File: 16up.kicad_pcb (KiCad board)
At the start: 2 copper layers, 60.8 x 99.9 mm, 38 parts, among them CN1 EXPANSION_PORT, CN2 ALMOST_USERPORT, CN3 DB9_MALE, J1 ATTENTION_IN, J2 TAPE_IN, U1 GAL20V8, U102 74LS652, U2 MOS_6529, U3 MOS_6551_ACIA, U4 MAX238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

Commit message: ExtraUserPort -> 16up
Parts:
- CN1: footprint ExtraUserPort:C16_Cart_Conn -> 16up:C16_Cart_Conn
- CN2: footprint ExtraUserPort:24Pin_Edge -> 16up:24Pin_Edge
- CN3: footprint ExtraUserPort:DB_9M -> 16up:DB_9M
- J2: footprint ExtraUserPort:Connector_Mini-DIN_Female_8Pin_2rows -> 16up:Connector_Mini-DIN_Female_8Pin_2rows
- V0: footprint ExtraUserPort:logo -> 16up:logo
- V1: footprint ExtraUserPort:cc_by_nc_sa -> 16up:cc_by_nc_sa

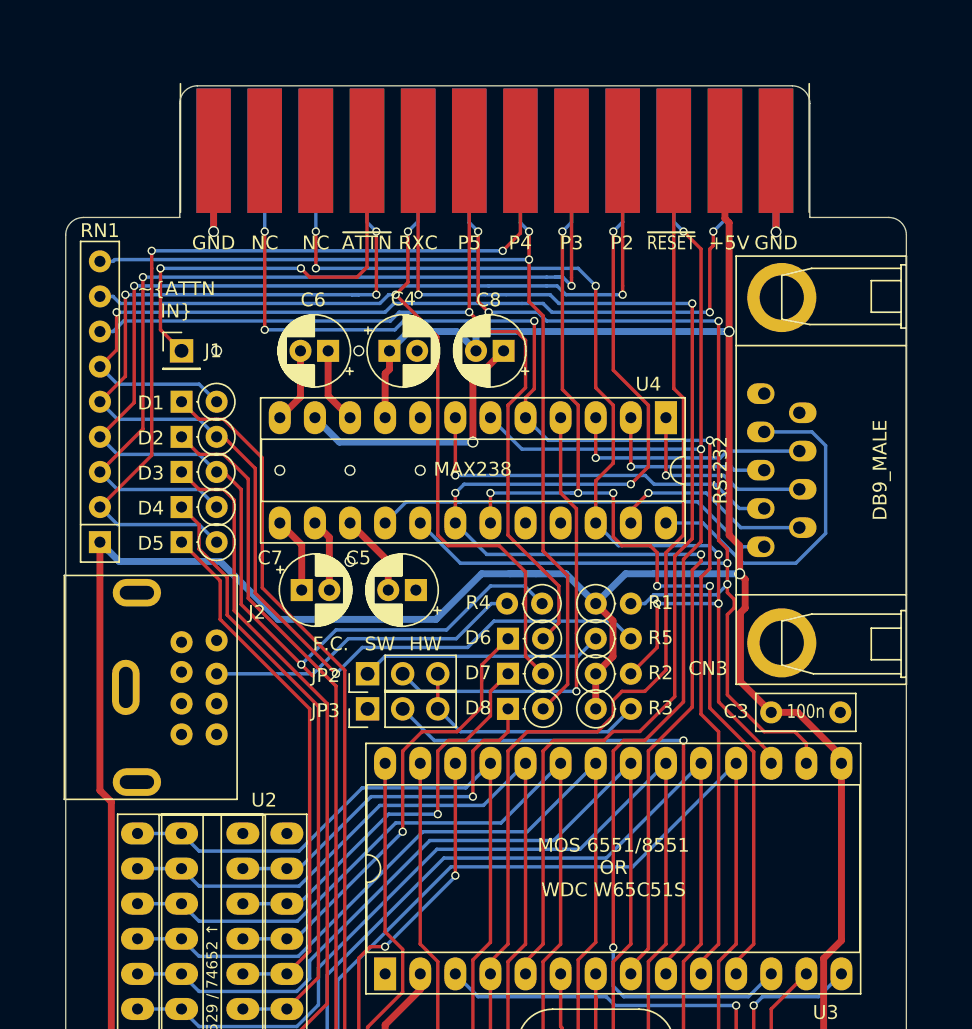
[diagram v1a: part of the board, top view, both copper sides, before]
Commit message: Fix userport connector !!!
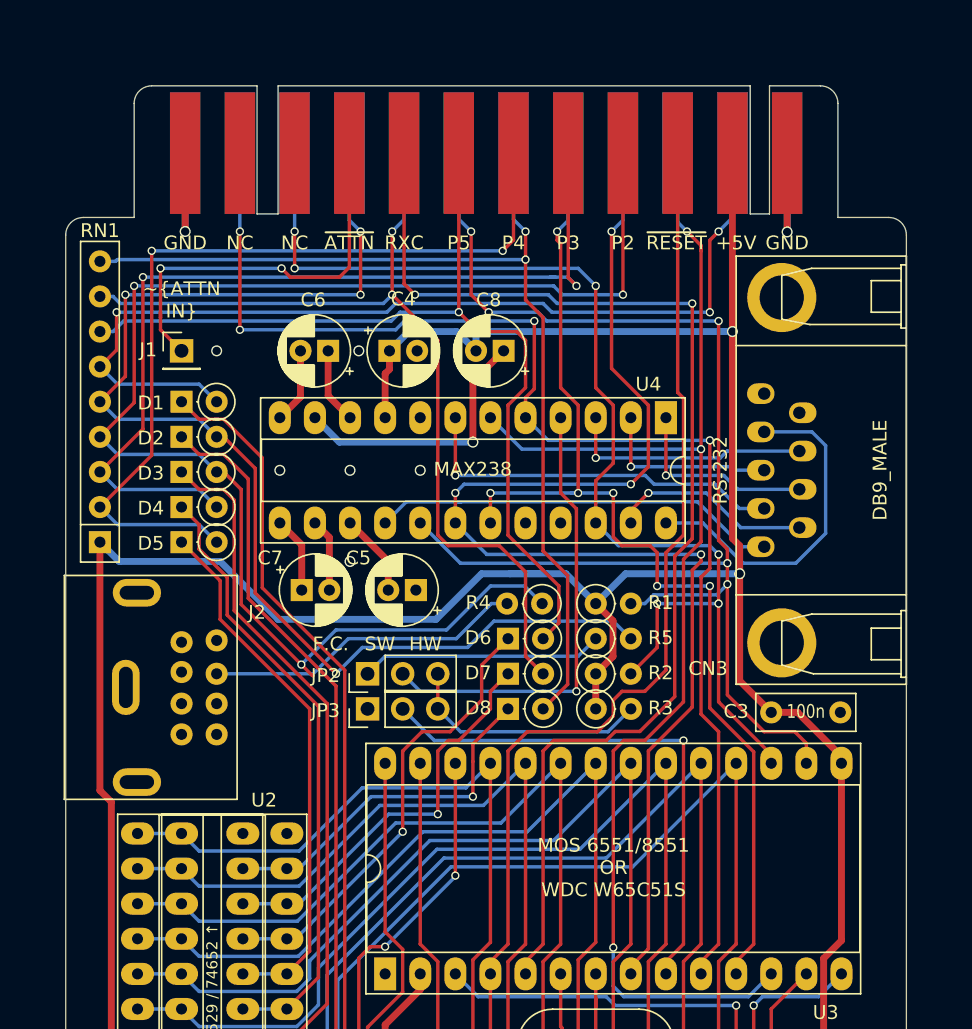
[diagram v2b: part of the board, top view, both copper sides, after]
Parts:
- CN2: footprint 16up:24Pin_Edge -> 16up:Plus4_UserPort
- moved CN2 21.2 mm to (152.2, 57.7)
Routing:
- net /pc2: track 110.0 -> 105.5 mm
- net /~dcd_ttl: track 96.8 -> 100.8 mm
- net /pc1: track 91.9 -> 89.9 mm
- net /txd_ttl: track 94.0 -> 95.6 mm
- net /~dsr_ttl: track 86.2 -> 87.7 mm
- net Net-(CN2-Pad9): track 30.9 -> 29.5 mm
- net /pc6: track 67.1 -> 66.3 mm
- net /p7: track 27.4 -> 26.7 mm
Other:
- outline, holes or cut-outs redrawn

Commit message: Final touches
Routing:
- net GND: vias 12 -> 11

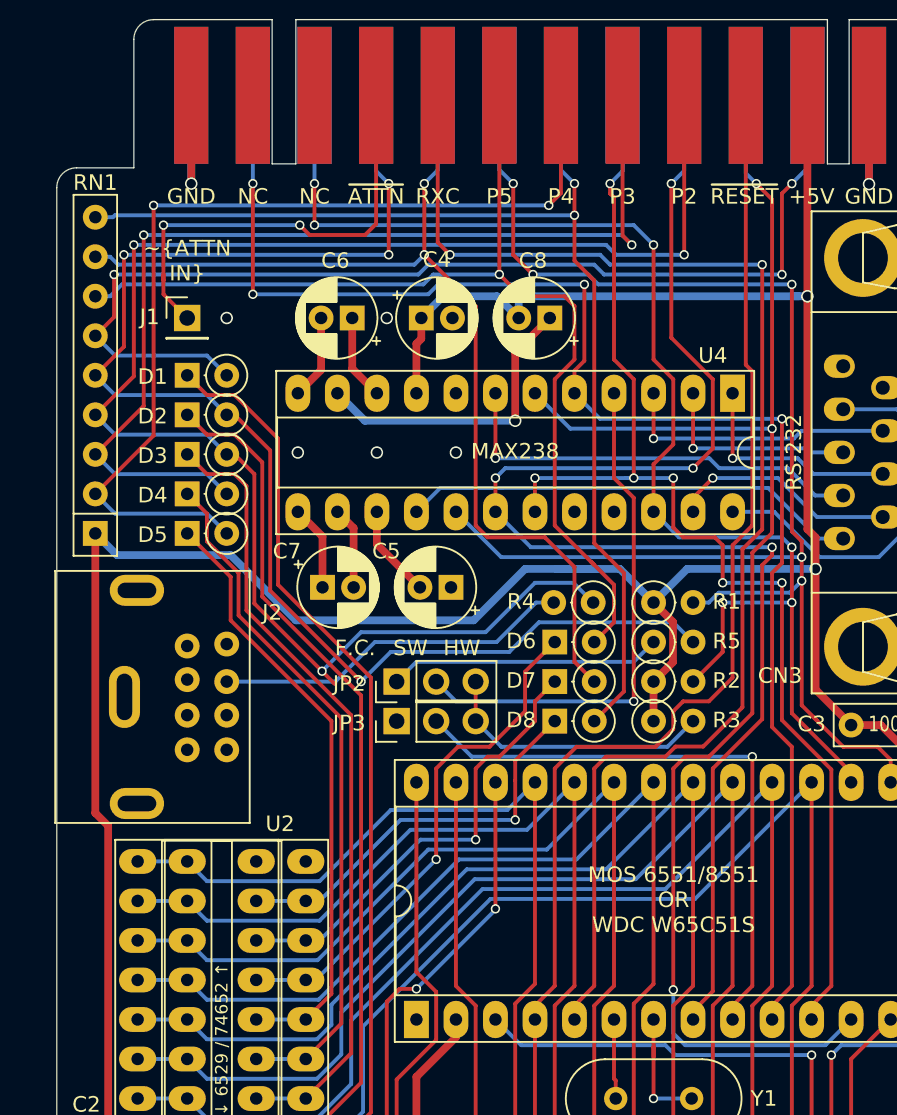
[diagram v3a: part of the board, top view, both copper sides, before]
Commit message: Remove serial signals from Userport connector They wouldn't work anyway, as whatever gets connected there expects all control signals to be inverted as per Commodore serial port standards.
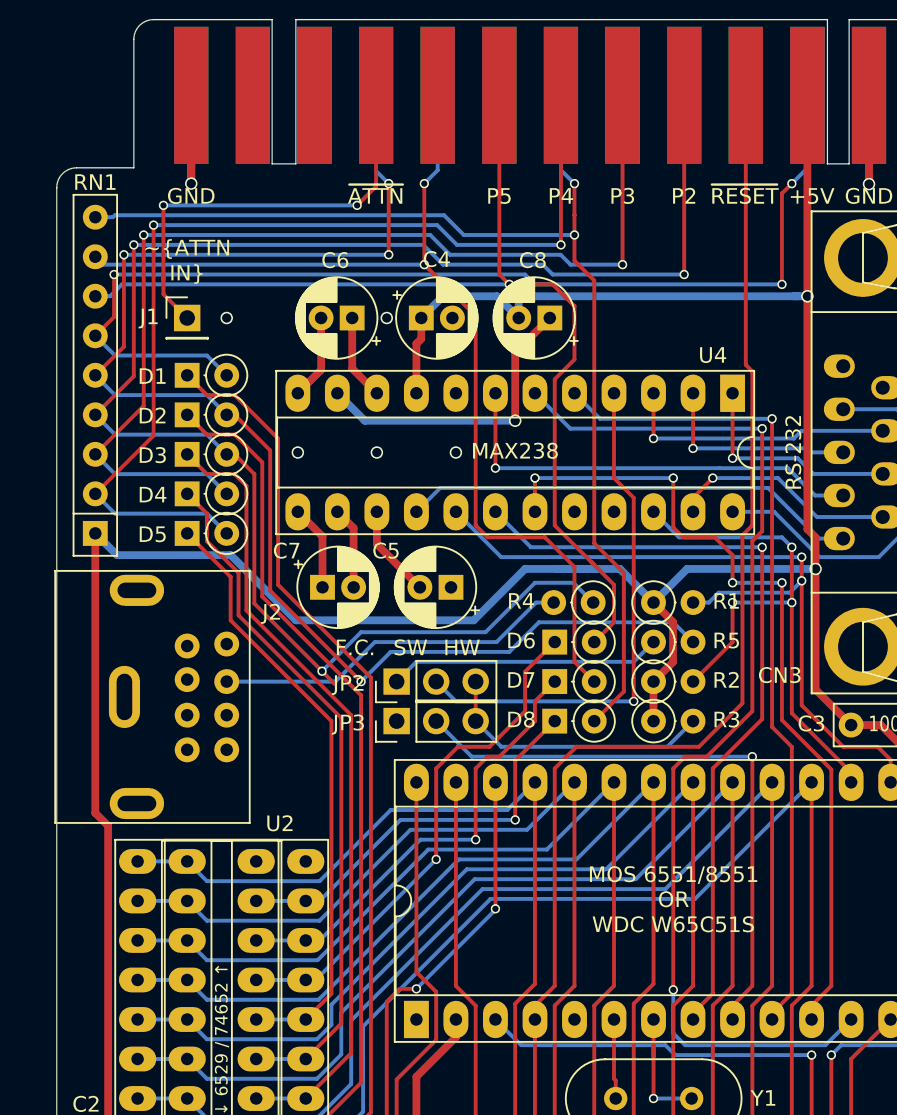
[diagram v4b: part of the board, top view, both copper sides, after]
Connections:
- CN2 pad 8: /rxc_ttl -> (no net)
- CN2 pad C: /rxd_ttl -> (no net)
- CN2 pad D: /~rts_ttl -> (no net)
- CN2 pad E: /~dtr_ttl -> (no net)
- CN2 pad H: /~dcd_ttl -> (no net)
- CN2 pad L: /~dsr_ttl -> (no net)
- CN2 pad M: /txd_ttl -> (no net)
- U3 pad 5: /rxc_ttl -> (no net)
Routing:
- net /rxc_ttl: track 87.7 -> 0.00 mm, vias 2 -> 0
- net /~dcd_ttl: track 100.8 -> 49.4 mm, vias 5 -> 2
- net /~dsr_ttl: track 87.7 -> 38.4 mm, vias 6 -> 3
- net /txd_ttl: track 95.6 -> 53.0 mm, vias 4 -> 1
- net /~rts_ttl: track 92.3 -> 50.3 mm, vias 4 -> 1
- net /~dtr_ttl: track 80.1 -> 53.6 mm, vias 6 -> 4
- net /rxd_ttl: track 93.2 -> 70.0 mm, vias 3 -> 2
- net /pc4: track 62.4 -> 64.6 mm
- net /pc2: track 105.5 -> 107.3 mm
- net Net-(CN2-Pad9): track 29.5 -> 28.3 mm
- net /~reset: track 116.3 -> 117.0 mm
- net /pc3: track 66.8 -> 67.3 mm
- net /pc7: track 73.5 -> 74.1 mm
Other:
- board text removed: "NC"
- board text removed: "RXC"
- board text removed: "RXD"
- board text removed: "TXD"
- board text removed: "~DCD"
- board text removed: "~DSR"
- board text removed: "~DTR"
- board text removed: "~RTS"

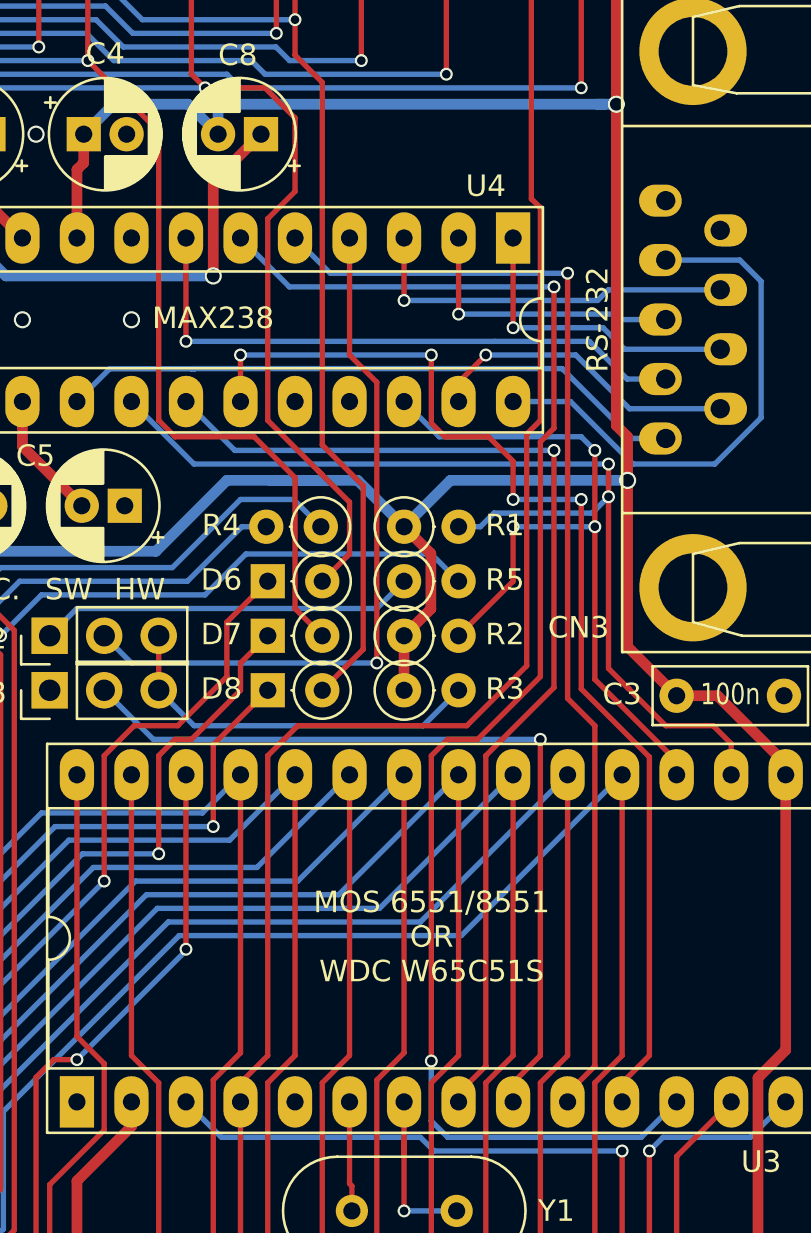
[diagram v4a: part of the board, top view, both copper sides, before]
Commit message: Pull-up signals at the RS-232 port
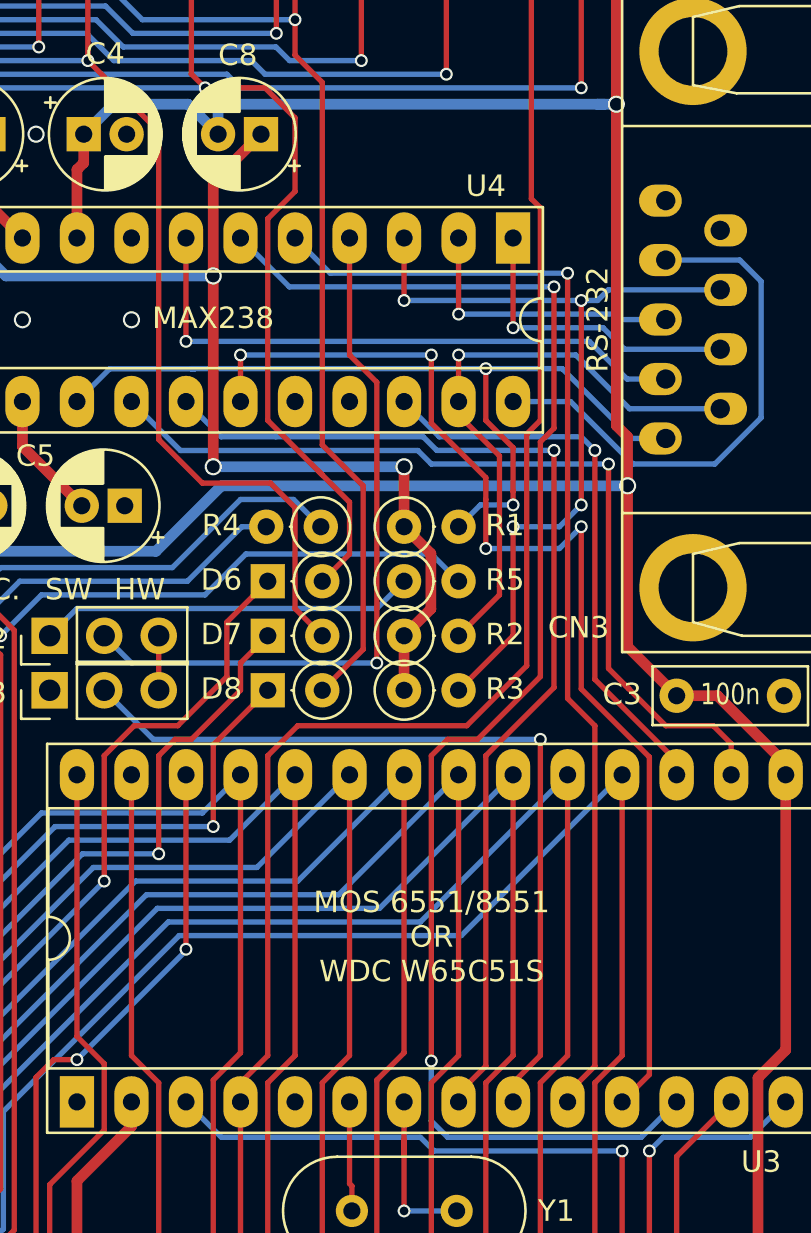
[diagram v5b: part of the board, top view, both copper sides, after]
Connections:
- C8 pad 1: Net-(C8-Pad1) -> +12V
- R1 pad 1: +5V -> +12V
- R1 pad 2: /~dcd_ttl -> /~dcd
- R2 pad 1: +5V -> +12V
- R2 pad 2: /~dsr_ttl -> /~dsr
- R3 pad 1: +5V -> +12V
- R3 pad 2: /~cts_ttl -> /~cts
- U4 pad 11: Net-(C8-Pad1) -> +12V
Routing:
- net +12V: track 0.00 -> 48.9 mm, vias 0 -> 3
- net /~cts: track 17.8 -> 39.6 mm, vias 1 -> 4
- net Net-(C8-Pad1): track 19.7 -> 0.00 mm, vias 1 -> 0
- net /~cts_ttl: track 17.9 -> 2.54 mm
- net /~dsr: track 14.7 -> 27.9 mm
- net +5V: track 304.8 -> 291.6 mm
- net /~dsr_ttl: track 38.4 -> 28.4 mm, vias 3 -> 1
- net /~dcd: track 29.6 -> 39.4 mm, vias 0 -> 2
- net /~dcd_ttl: track 49.4 -> 41.8 mm, vias 2 -> 1
- net /~dtr_ttl: track 53.6 -> 54.6 mm
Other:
- board text added: "THANKS TO ALL THE FOLKS AT THE PLUS/4 WORLD FORUM!"
- board text removed: "THANKS TO THE FOLKS FROM THE PLUS/4 WORLD FORUM!"

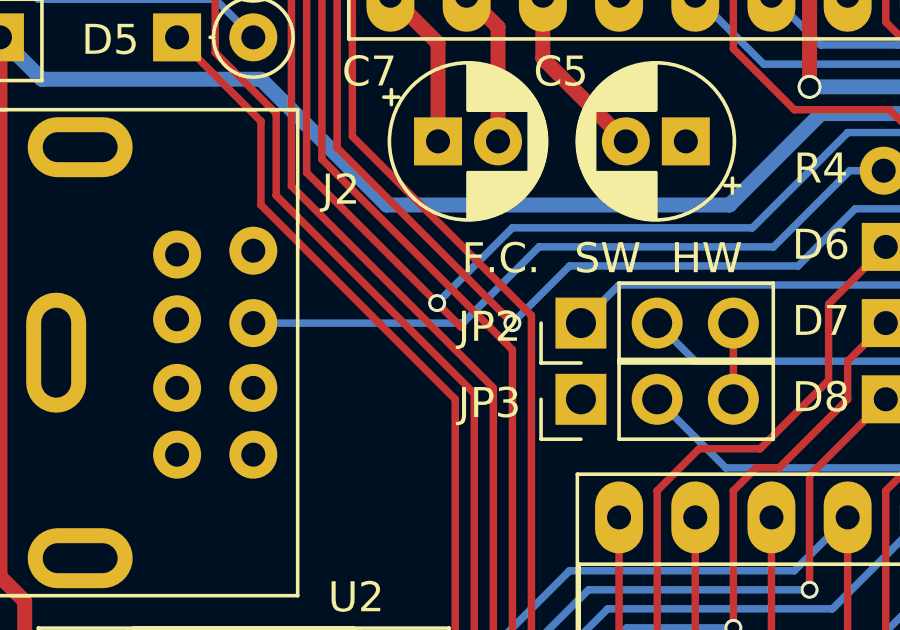
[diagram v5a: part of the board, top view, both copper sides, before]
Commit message: Get rid of protruding track
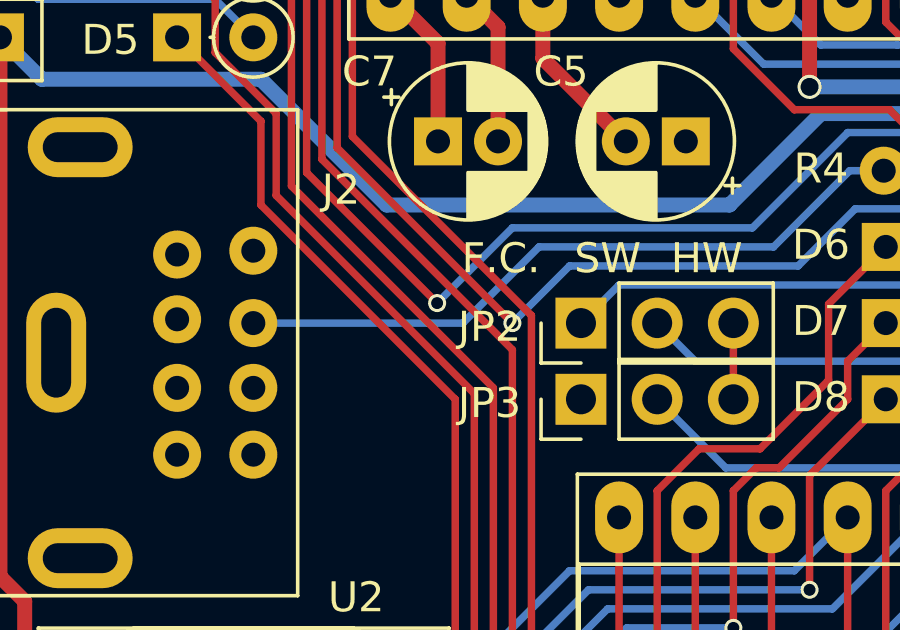
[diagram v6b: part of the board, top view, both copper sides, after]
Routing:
- net /pc2: track 107.3 -> 106.1 mm
